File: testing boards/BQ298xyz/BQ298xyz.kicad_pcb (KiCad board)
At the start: 2 copper layers, 8 parts, among them U1 1048-2S-18650-Holder, U2 BQ298xyz, U3 DMN3016LFDE, U4 DMN3016LFDE

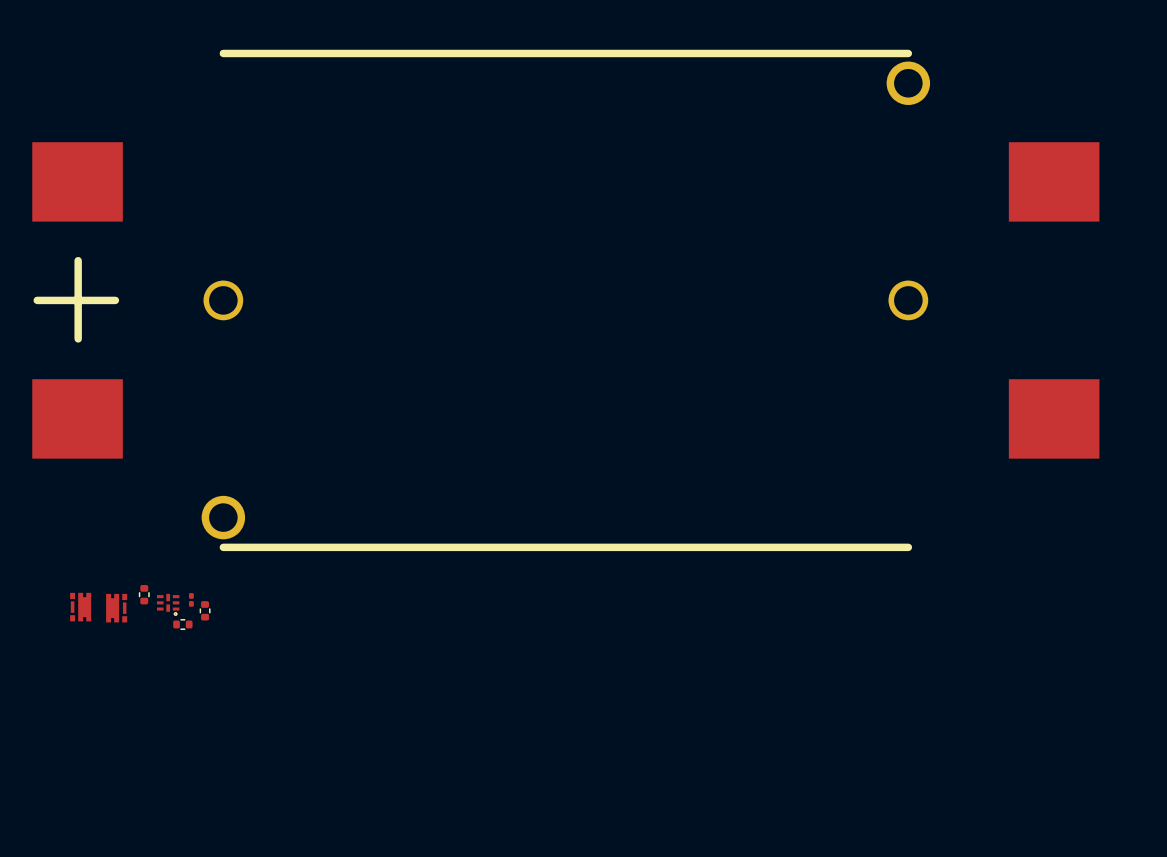
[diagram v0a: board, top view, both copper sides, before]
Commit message: Finished Battery Protection Board
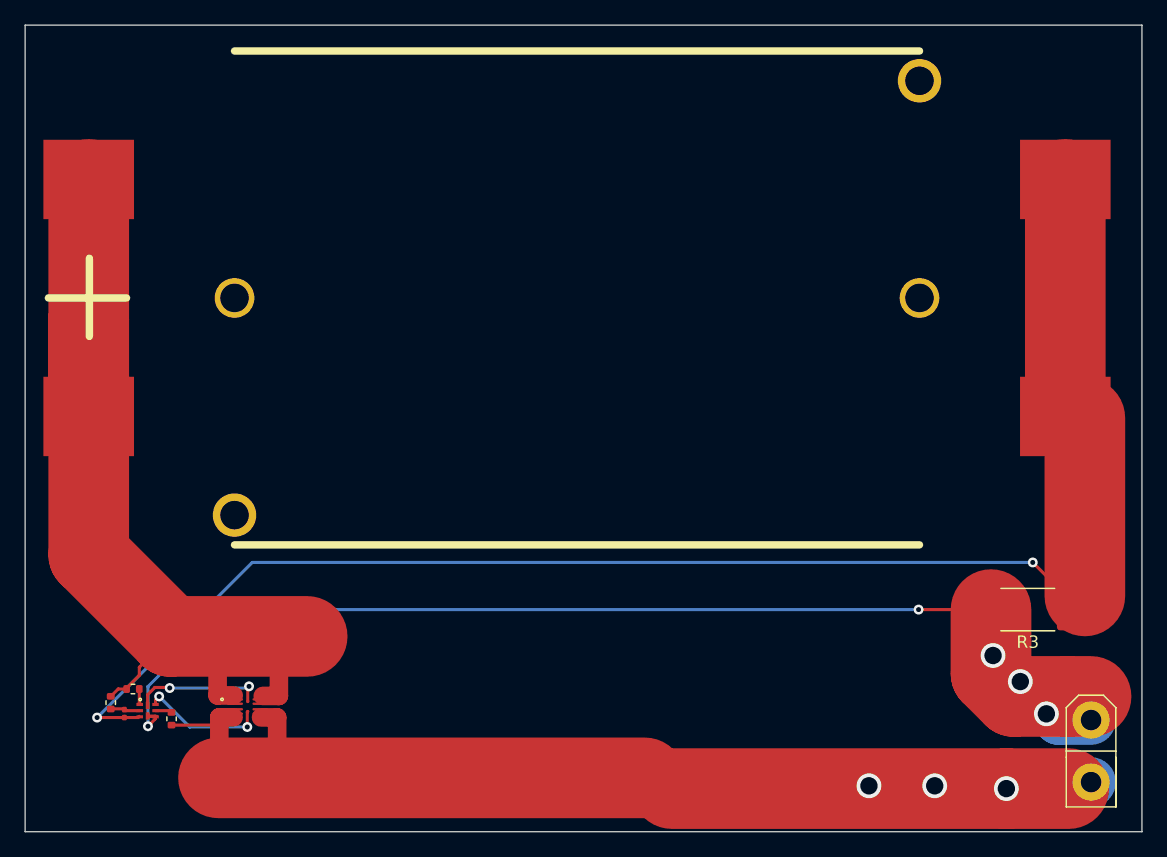
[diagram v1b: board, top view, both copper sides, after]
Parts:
- removed U4: DMN3016LFDE, HS2_parts:U-DFN2020-6
- added J1: XT30, HS2_parts:XT30, F.Cu at (190.9, 126.0)
- added R3: 1mOhm, Resistor_SMD:R_2512_6332Metric, F.Cu at (185.8, 112.1)
- U3: value DMN3016LFDE -> EFC2K103NUZTDG; footprint HS2_parts:U-DFN2020-6 -> HS2_parts:EFC2K103NUZTDG
- moved U3 13.7 mm to (122.9, 119.9)
- moved C1 10.6 mm to (113.0, 120.5), turned to 270 degrees
- moved R1 10.6 mm to (111.9, 119.6), turned to 270 degrees
- moved R4 10.2 mm to (116.8, 120.9), turned to 90 degrees
- moved U2 8.85 mm to (114.9, 120.2), turned to 270 degrees
- moved R2 6.57 mm to (113.7, 118.5), turned to 0 degrees
- moved U1 0.92 mm to (121.9, 87.0)
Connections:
- U3 pad 1: Net-(U3-Pad1) -> /BATT+
- U3 pad 2: /BATT+ -> /PACK+
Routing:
- net /BATT-: track 0.00 -> 122.9 mm, vias 0 -> 2
- net /PACK-: track 0.00 -> 100.5 mm, vias 0 -> 5
- net /PACK+: track 0.00 -> 96.3 mm, vias 0 -> 3
- net /BATT+: track 0.00 -> 72.0 mm
- net /CHG: track 0.00 -> 10.6 mm, vias 0 -> 2
- net Net-(U2-Pad7): track 0.00 -> 10.4 mm, vias 0 -> 2
- net Net-(C1-Pad1): track 0.00 -> 2.50 mm
- net Net-(R4-Pad2): track 0.00 -> 1.31 mm
- net Net-(R2-Pad2): track 0.00 -> 1.24 mm
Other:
- board outline added: 90 x 65 mm
